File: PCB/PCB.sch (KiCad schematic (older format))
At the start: 31 parts, among them J1 BME280, J2 ATTINY24, J3 ATTINY85, J4 ATTINY85, J5 ATTINY24, J5 Wind, J6 Rain, J6 ReedSwitches-WindVane, U1 MCP1702-5002E_TO92 5V, U2 MCP1700-3302E_TO92 3.3V, U3 ATtiny85-20PU Wind, U4 ATtiny85-20PU Bat, U5 ATtiny24A-PU WindDir

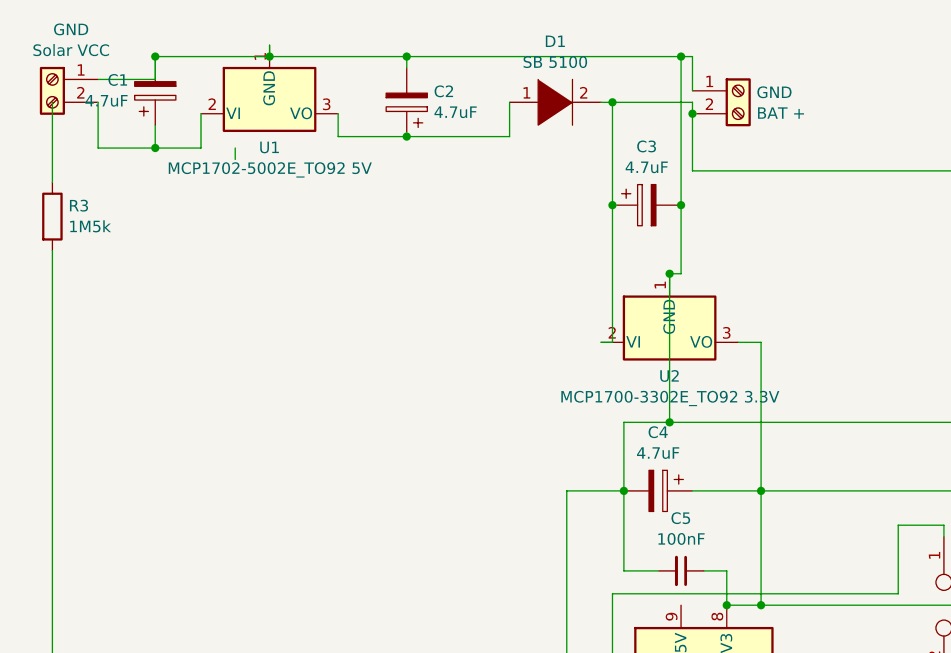
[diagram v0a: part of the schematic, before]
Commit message: Schematics Update
Schematics update, now working I2C Communication. New Code for ATTINYs (less overhead)
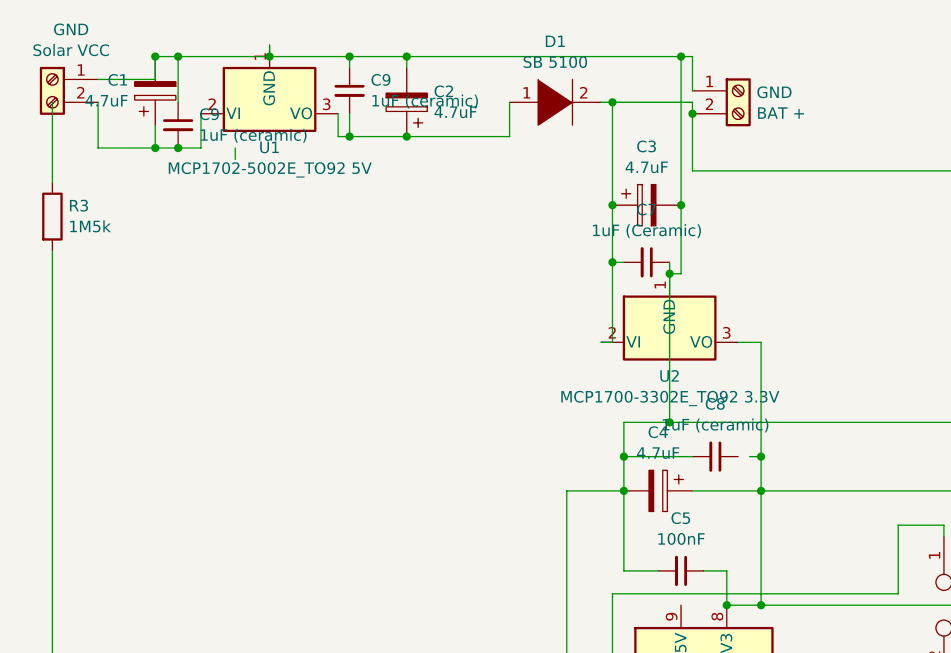
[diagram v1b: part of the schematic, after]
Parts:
- added C7: 1uF (Ceramic), symbol Device:C_Small
- added C8, C9 (x2): 1uF (ceramic), symbol Device:C_Small
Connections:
- wire segments 184 -> 198
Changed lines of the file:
@@
 EESchema Schematic File Version 4
+LIBS:PCB-cache
 EELAYER 29 0
 EELAYER END
@@
 	1550 1200 1550 1050
 Wire Wire Line
-	1350 1200 1550 1200
+	1350 1200 1450 1200
 Wire Wire Line
 	1100 900  1350 900
 Wire Wire Line
-	1350 800  1850 800
+	1350 800  1450 800
 Wire Wire Line
 	1850 800  1850 750
@@
 $EndComp
 Wire Wire Line
-	1850 800  2450 800
+	1850 800  2200 800
 Wire Wire Line
 	2450 800  2450 850
 Connection ~ 1850 800
 Wire Wire Line
-	2450 1150 2150 1150
+	2450 1150 2200 1150
 Wire Wire Line
 	2150 1150 2150 1050
@@
 $EndComp
 Wire Wire Line
-	3350 1450 3350 2050
+	3350 1450 3350 1700
 Wire Wire Line
 	3350 2050 3300 2050
@@
 	3700 2700 4000 2700
 Wire Wire Line
-	4000 2700 4000 2050
-Wire Wire Line
-	3400 2700 3400 2400
+	4000 2700 4000 2550
+Wire Wire Line
+	3400 2700 3400 2550
 Wire Wire Line
 	3400 2400 3600 2400
@@
 Text Notes 7450 7500 0    50   ~ 0
 Wireless Weather
+$Comp
+L Device:C_Small C7
+U 1 1 5D33E396
+P 3500 1700
+F 0 "C7" V 3271 1700 50  0000 C CNN
+F 1 "1uF (Ceramic)" V 3362 1700 50  0000 C CNN
+F 2 "" H 3500 1700 50  0001 C CNN
+F 3 "~" H 3500 1700 50  0001 C CNN
+	1    3500 1700
+	0    1    1    0
+$EndComp
+Wire Wire Line
+	3600 1750 3600 1700
+Wire Wire Line
+	3400 1700 3350 1700
+Connection ~ 3350 1700
+Wire Wire Line
+	3350 1700 3350 2050
+$Comp
+L Device:C_Small C8
+U 1 1 5D350CBD
+P 3800 2550
+F 0 "C8" V 3571 2550 50  0000 C CNN
+F 1 "1uF (ceramic)" V 3662 2550 50  0000 C CNN
+F 2 "" H 3800 2550 50  0001 C CNN
+F 3 "~" H 3800 2550 50  0001 C CNN
+	1    3800 2550
+	0    1    1    0
+$EndComp
+Wire Wire Line
+	3950 2550 4000 2550
+Connection ~ 4000 2550
+Wire Wire Line
+	4000 2550 4000 2050
+Wire Wire Line
+	3700 2550 3400 2550
+Connection ~ 3400 2550
+Wire Wire Line
+	3400 2550 3400 2400
+$Comp
+L Device:C_Small C9
+U 1 1 5D3626CA
+P 2200 950
+F 0 "C9" H 2292 996 50  0000 L CNN
+F 1 "1uF (ceramic)" H 2292 905 50  0000 L CNN
+F 2 "" H 2200 950 50  0001 C CNN
+F 3 "~" H 2200 950 50  0001 C CNN
+	1    2200 950
+	1    0    0    -1
+$EndComp
+$Comp
+L Device:C_Small C9
+U 1 1 5D3637F6
+P 1450 1100
+F 0 "C9" H 1542 1146 50  0000 L CNN
+F 1 "1uF (ceramic)" H 1542 1055 50  0000 L CNN
+F 2 "" H 1450 1100 50  0001 C CNN
+F 3 "~" H 1450 1100 50  0001 C CNN
+	1    1450 1100
+	1    0    0    -1
+$EndComp
+Connection ~ 1450 1200
+Wire Wire Line
+	1450 1200 1550 1200
+Wire Wire Line
+	1450 1000 1450 800
+Connection ~ 1450 800
+Wire Wire Line
+	1450 800  1850 800
+Wire Wire Line
+	2200 850  2200 800
+Connection ~ 2200 800
+Wire Wire Line
+	2200 800  2450 800
+Wire Wire Line
+	2200 1050 2200 1150
+Connection ~ 2200 1150
+Wire Wire Line
+	2200 1150 2150 1150
 $EndSCHEMATC

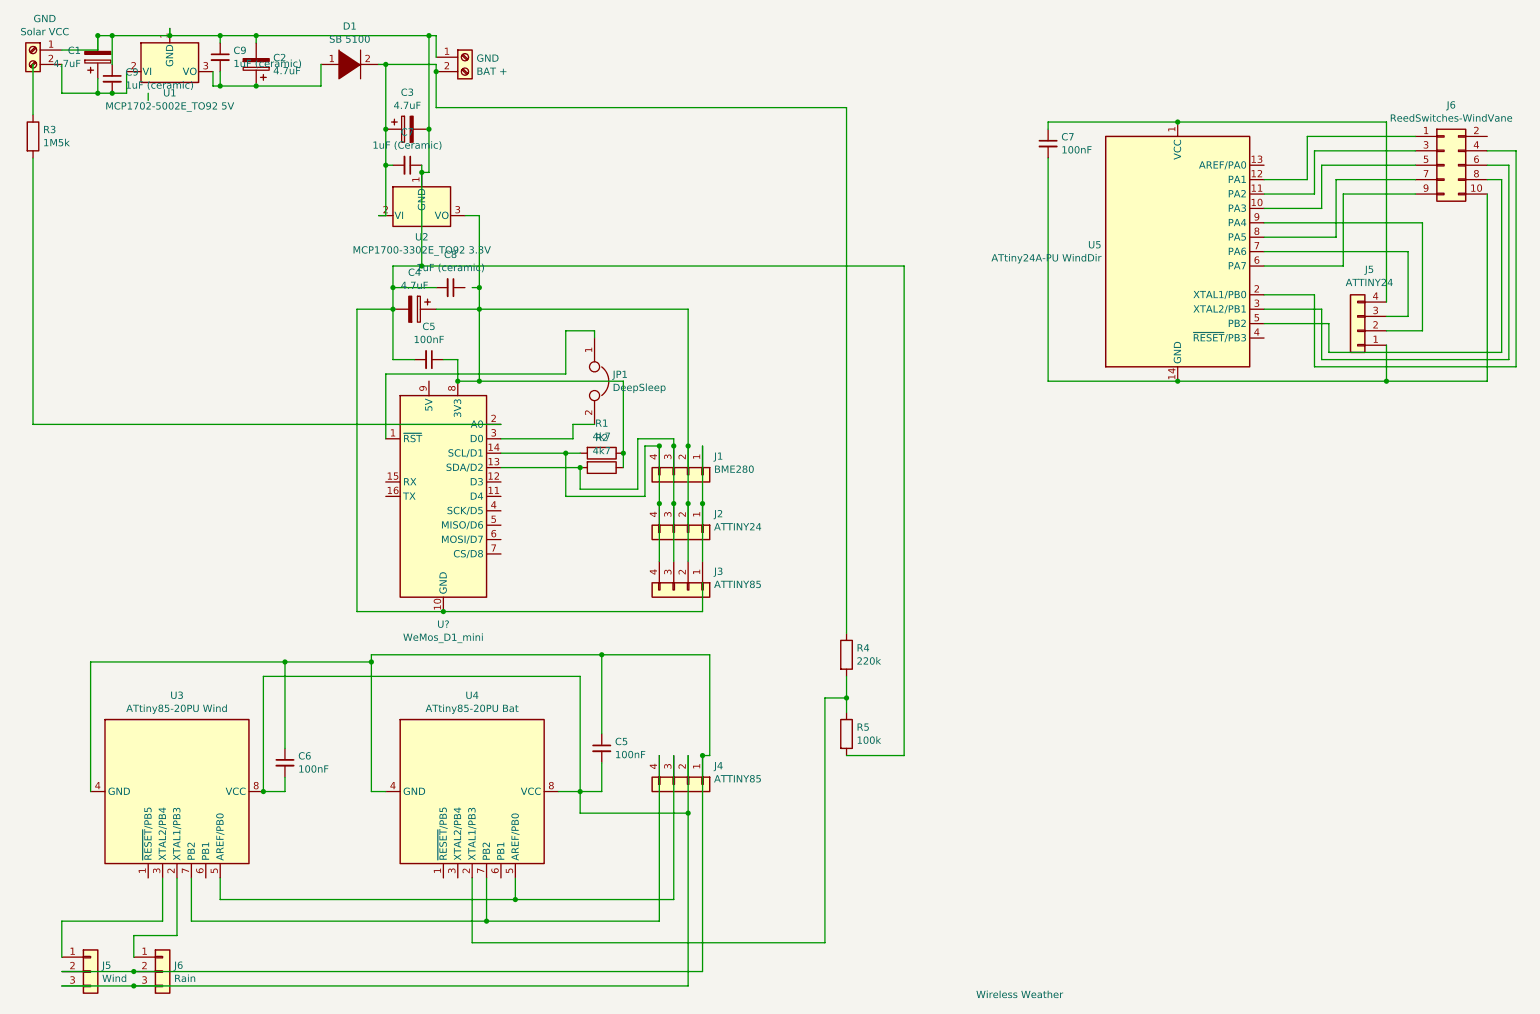
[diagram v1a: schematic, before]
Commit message: Small fixes, Solar power added
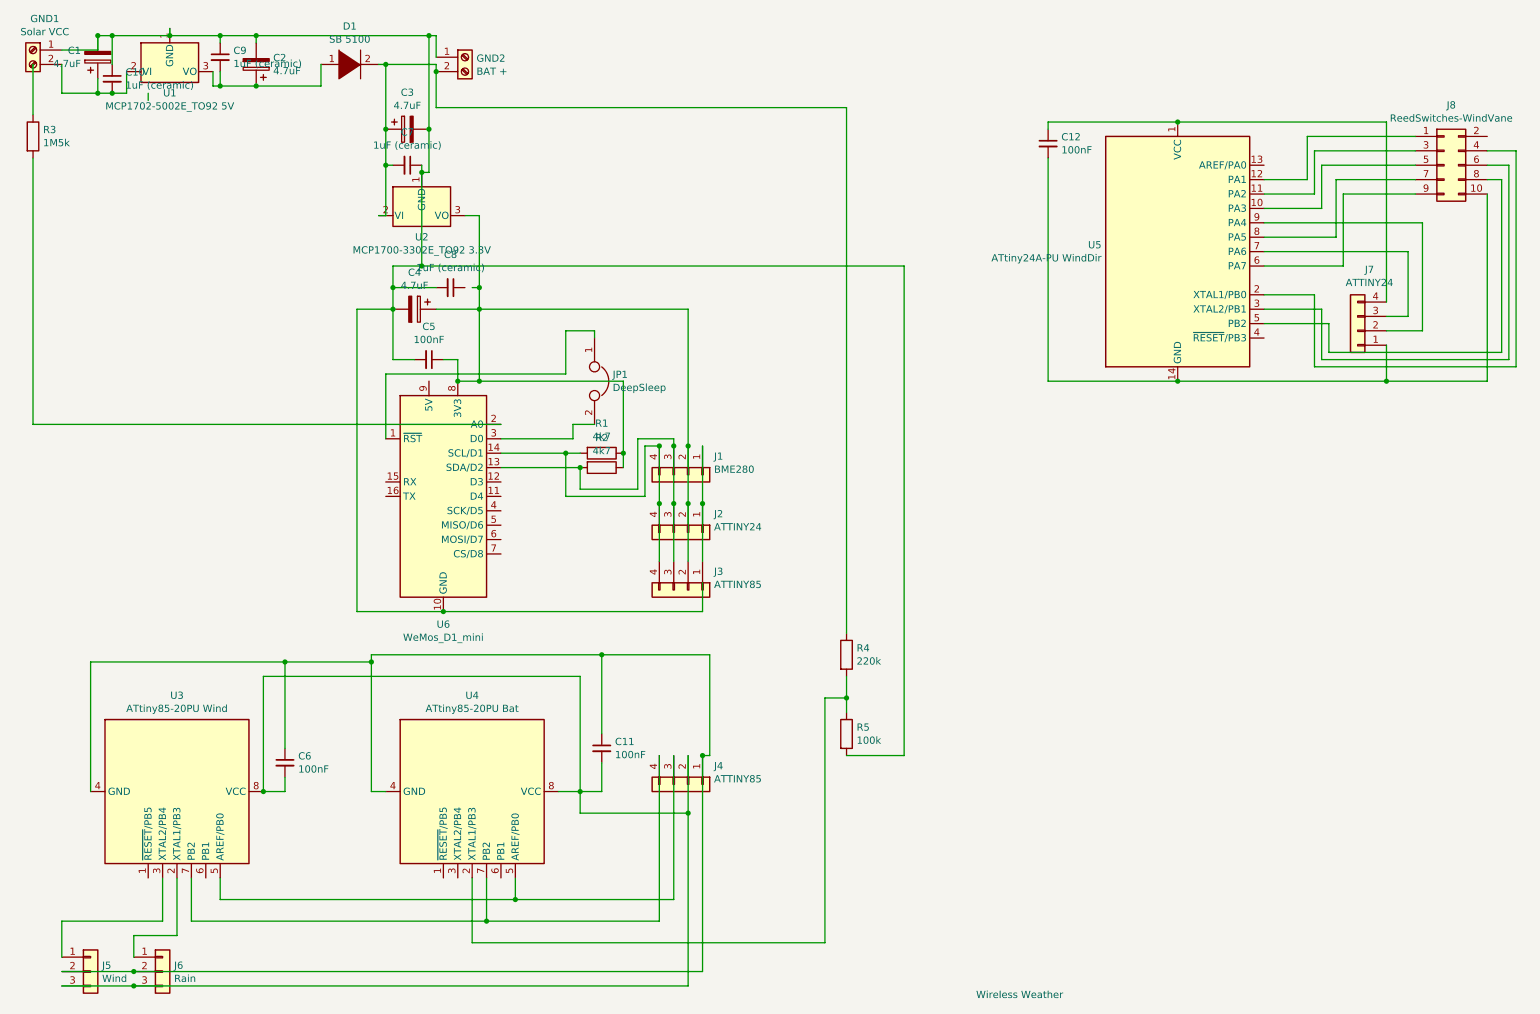
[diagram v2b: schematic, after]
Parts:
- C7: value 1uF (Ceramic) -> 1uF (ceramic)
- gave numbers to parts that had none: 1
- renumbered C9 to C10, C5 to C11, C7 to C12, GND to GND1, GND to GND2, J5 to J7, J6 to J8
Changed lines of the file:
@@
 $EndDescr
 $Comp
-L Connector:Screw_Terminal_01x02 GND
+L Connector:Screw_Terminal_01x02 GND1
 U 1 1 5D2E117A
 P 900 900
-F 0 "GND" H 818 1117 50  0000 C CNN
+F 0 "GND1" H 818 1117 50  0000 C CNN
 F 1 "Solar VCC" H 818 1026 50  0000 C CNN
 F 2 "" H 900 900 50  0001 C CNN
@@
 Connection ~ 2450 1150
 $Comp
-L Connector:Screw_Terminal_01x02 GND
+L Connector:Screw_Terminal_01x02 GND2
 U 1 1 5D2EAFA5
 P 3900 950
-F 0 "GND" H 3980 942 50  0000 L CNN
+F 0 "GND2" H 3980 942 50  0000 L CNN
 F 1 "BAT +" H 3980 851 50  0000 L CNN
 F 2 "" H 3900 950 50  0001 C CNN
@@
 Connection ~ 3600 1750
 $Comp
-L MCU_Module:WeMos_D1_mini U?
+L MCU_Module:WeMos_D1_mini U6
 U 1 1 5D2F24FC
 P 3750 4000
-F 0 "U?" H 3750 3111 50  0000 C CNN
+F 0 "U6" H 3750 3111 50  0000 C CNN
 F 1 "WeMos_D1_mini" H 3750 3020 50  0000 C CNN
 F 2 "Module:WEMOS_D1_mini_light" H 3750 2850 50  0001 C CNN
@@
 $EndComp
 $Comp
-L Device:C_Small C5
+L Device:C_Small C11
 U 1 1 5D3244AF
 P 4850 5750
-F 0 "C5" H 4942 5796 50  0000 L CNN
+F 0 "C11" H 4942 5796 50  0000 L CNN
 F 1 "100nF" H 4942 5705 50  0000 L CNN
 F 2 "" H 4850 5750 50  0001 C CNN
@@
 $EndComp
 $Comp
-L Device:C_Small C7
+L Device:C_Small C12
 U 1 1 5D3763C4
 P 7950 1550
-F 0 "C7" H 8042 1596 50  0000 L CNN
+F 0 "C12" H 8042 1596 50  0000 L CNN
 F 1 "100nF" H 8042 1505 50  0000 L CNN
 F 2 "" H 7950 1550 50  0001 C CNN
@@
 	7950 3200 8850 3200
 $Comp
-L Connector_Generic:Conn_01x04 J5
+L Connector_Generic:Conn_01x04 J7
 U 1 1 5D381A15
 P 10100 2850
-F 0 "J5" H 10018 2425 50  0000 C CNN
+F 0 "J7" H 10018 2425 50  0000 C CNN
 F 1 "ATTINY24" H 10018 2516 50  0000 C CNN
 F 2 "" H 10100 2850 50  0001 C CNN
@@
 	10450 2300 9450 2300
 $Comp
-L Connector_Generic:Conn_02x05_Odd_Even J6
+L Connector_Generic:Conn_02x05_Odd_Even J8
 U 1 1 5D3AFF2F
 P 10700 1700
-F 0 "J6" H 10750 2117 50  0000 C CNN
+F 0 "J8" H 10750 2117 50  0000 C CNN
 F 1 "ReedSwitches-WindVane" H 10750 2026 50  0000 C CNN
 F 2 "" H 10700 1700 50  0001 C CNN
@@
 P 3500 1700
 F 0 "C7" V 3271 1700 50  0000 C CNN
-F 1 "1uF (Ceramic)" V 3362 1700 50  0000 C CNN
+F 1 "1uF (ceramic)" V 3362 1700 50  0000 C CNN
 F 2 "" H 3500 1700 50  0001 C CNN
 F 3 "~" H 3500 1700 50  0001 C CNN
@@
 $EndComp
 $Comp
-L Device:C_Small C9
+L Device:C_Small C10
 U 1 1 5D3637F6
 P 1450 1100
-F 0 "C9" H 1542 1146 50  0000 L CNN
+F 0 "C10" H 1542 1146 50  0000 L CNN
 F 1 "1uF (ceramic)" H 1542 1055 50  0000 L CNN
 F 2 "" H 1450 1100 50  0001 C CNN
